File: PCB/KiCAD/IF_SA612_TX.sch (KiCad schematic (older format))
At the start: 19 parts, among them J3 MIC, Q10 MMBT4401LT1G, U8 LM78L06, U9 SA612

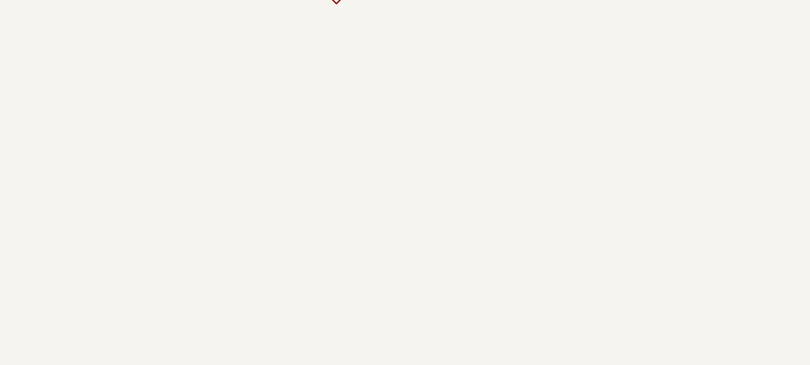
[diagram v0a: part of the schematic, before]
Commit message: diode mixer on discrete components, begin move to DragonFly libs
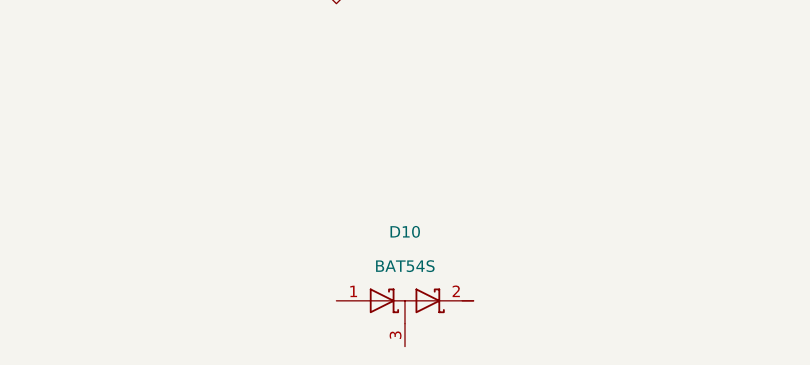
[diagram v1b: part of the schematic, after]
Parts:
- added D10: BAT54S, TO_SOT_Packages_SMD:SOT-23, symbol D_Schottky_x2_Serial_AKC
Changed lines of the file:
@@
 EESchema Schematic File Version 2
 LIBS:DragonFly-rescue
-LIBS:bee-rescue
 LIBS:power
 LIBS:device
@@
 $EndDescr
 $Comp
-L GND #PWR72
+L GND #PWR078
 U 1 1 58E1AB18
 P 1750 2050
-F 0 "#PWR72" H 1750 1800 50  0001 C CNN
+F 0 "#PWR078" H 1750 1800 50  0001 C CNN
 F 1 "GND" H 1750 1900 50  0001 C CNN
 F 2 "" H 1750 2050 50  0000 C CNN
@@
 $EndComp
 $Comp
-L GND #PWR74
+L GND #PWR079
 U 1 1 58E1AB3A
 P 2950 4000
-F 0 "#PWR74" H 2950 3750 50  0001 C CNN
+F 0 "#PWR079" H 2950 3750 50  0001 C CNN
 F 1 "GND" H 2950 3850 50  0001 C CNN
 F 2 "" H 2950 4000 50  0000 C CNN
@@
 $EndComp
 $Comp
-L GND #PWR73
+L GND #PWR080
 U 1 1 58E1AB40
 P 2200 4000
-F 0 "#PWR73" H 2200 3750 50  0001 C CNN
+F 0 "#PWR080" H 2200 3750 50  0001 C CNN
 F 1 "GND" H 2200 3850 50  0001 C CNN
 F 2 "" H 2200 4000 50  0000 C CNN
@@
 $EndComp
 $Comp
-L GND #PWR76
+L GND #PWR081
 U 1 1 58E1AB6A
 P 3250 1450
-F 0 "#PWR76" H 3250 1200 50  0001 C CNN
+F 0 "#PWR081" H 3250 1200 50  0001 C CNN
 F 1 "GND" H 3250 1300 50  0001 C CNN
 F 2 "" H 3250 1450 50  0000 C CNN
@@
 $EndComp
 $Comp
-L GND #PWR80
+L GND #PWR082
 U 1 1 58E1AB77
 P 5100 2050
-F 0 "#PWR80" H 5100 1800 50  0001 C CNN
+F 0 "#PWR082" H 5100 1800 50  0001 C CNN
 F 1 "GND" H 5100 1900 50  0001 C CNN
 F 2 "" H 5100 2050 50  0000 C CNN
@@
 $EndComp
 $Comp
-L GND #PWR79
+L GND #PWR083
 U 1 1 58E1AB7D
 P 4950 2850
-F 0 "#PWR79" H 4950 2600 50  0001 C CNN
+F 0 "#PWR083" H 4950 2600 50  0001 C CNN
 F 1 "GND" H 4950 2700 50  0001 C CNN
 F 2 "" H 4950 2850 50  0000 C CNN
@@
 $EndComp
 $Comp
-L GND #PWR78
+L GND #PWR084
 U 1 1 58E1ABAE
 P 4800 1500
-F 0 "#PWR78" H 4800 1250 50  0001 C CNN
+F 0 "#PWR084" H 4800 1250 50  0001 C CNN
 F 1 "GND" H 4800 1350 50  0001 C CNN
 F 2 "" H 4800 1500 50  0000 C CNN
@@
 $EndComp
 $Comp
-L GND #PWR81
+L GND #PWR085
 U 1 1 58E1ABB4
 P 5300 1500
-F 0 "#PWR81" H 5300 1250 50  0001 C CNN
+F 0 "#PWR085" H 5300 1250 50  0001 C CNN
 F 1 "GND" H 5300 1350 50  0001 C CNN
 F 2 "" H 5300 1500 50  0000 C CNN
@@
 Connection ~ 5950 2250
 $Comp
-L GND #PWR82
+L GND #PWR086
 U 1 1 58E1ABEC
 P 5850 2400
-F 0 "#PWR82" H 5850 2150 50  0001 C CNN
+F 0 "#PWR086" H 5850 2150 50  0001 C CNN
 F 1 "GND" H 5850 2250 50  0001 C CNN
 F 2 "" H 5850 2400 50  0000 C CNN
@@
 	5850 2350 6050 2350
 $Comp
-L GND #PWR83
+L GND #PWR087
 U 1 1 58E1ABF4
 P 5850 2950
-F 0 "#PWR83" H 5850 2700 50  0001 C CNN
+F 0 "#PWR087" H 5850 2700 50  0001 C CNN
 F 1 "GND" H 5850 2800 50  0001 C CNN
 F 2 "" H 5850 2950 50  0000 C CNN
@@
 	2950 3800 2950 4000
 $Comp
-L GND #PWR77
+L GND #PWR088
 U 1 1 60FE7FDF
 P 3500 4250
-F 0 "#PWR77" H 3500 4000 50  0001 C CNN
+F 0 "#PWR088" H 3500 4000 50  0001 C CNN
 F 1 "GND" H 3500 4100 50  0001 C CNN
 F 2 "" H 3500 4250 50  0000 C CNN
@@
 $EndComp
 $Comp
-L GND #PWR75
+L GND #PWR089
 U 1 1 60FE877B
 P 3100 2600
-F 0 "#PWR75" H 3100 2350 50  0001 C CNN
+F 0 "#PWR089" H 3100 2350 50  0001 C CNN
 F 1 "GND" H 3100 2450 50  0001 C CNN
 F 2 "" H 3100 2600 50  0000 C CNN
@@
 Wire Wire Line
 	3500 2700 3500 3050
+$Comp
+L D_Schottky_x2_Serial_AKC D10
+U 1 1 612298E2
+P 3800 5650
+F 0 "D10" H 3800 5950 50  0000 C CNN
+F 1 "BAT54S" H 3800 5800 50  0000 C CNN
+F 2 "TO_SOT_Packages_SMD:SOT-23" H 3800 5650 50  0001 C CNN
+F 3 "" H 3800 5650 50  0000 C CNN
+	1    3800 5650
+	1    0    0    -1
+$EndComp
 $EndSCHEMATC

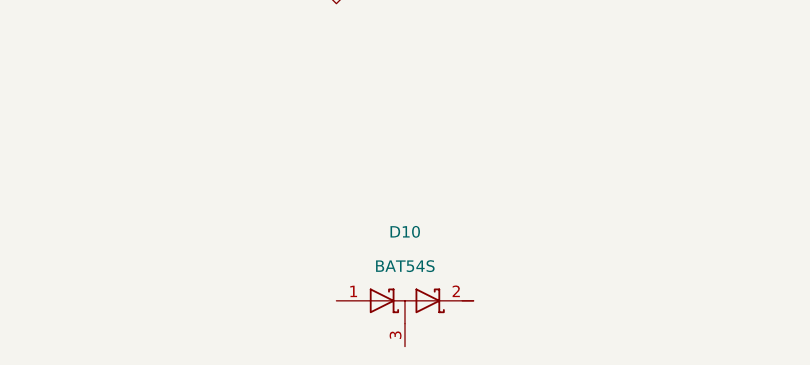
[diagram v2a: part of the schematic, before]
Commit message: PCB read works, layout BPF
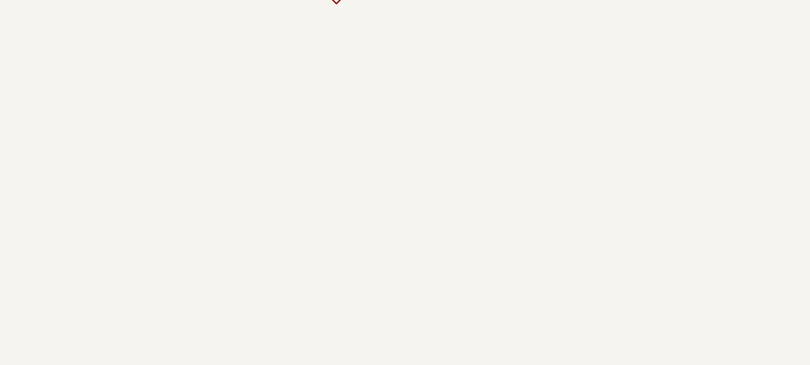
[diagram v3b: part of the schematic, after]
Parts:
- removed D10: BAT54S, TO_SOT_Packages_SMD:SOT-23, symbol D_Schottky_x2_Serial_AKC
- C32, C33, C35, C36, C38, C42: footprint Capacitors_SMD:C_0603_HandSoldering -> DragonFly:C_0603_HandSoldering
- C40: footprint Capacitors_THT:CP_Radial_D6.3mm_P2.50mm -> DragonFly:CP_Radial_D6.3mm_P2.50mm
- D5, Q10: footprint TO_SOT_Packages_SMD:SOT-23 -> DragonFly:SOT-23
- U8: footprint TO_SOT_Packages_THT:TO-92_Molded_Wide_Oval -> DragonFly:TO-92_Molded_Wide_Oval
- U9: footprint Housings_SOIC:SOIC-8_3.9x4.9mm_Pitch1.27mm -> DragonFly:SOIC-8_3.9x4.9mm_Pitch1.27mm
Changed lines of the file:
@@
 $EndDescr
 $Comp
-L GND #PWR78
+L GND #PWR078
 U 1 1 58E1AB18
 P 1750 2050
-F 0 "#PWR78" H 1750 1800 50  0001 C CNN
+F 0 "#PWR078" H 1750 1800 50  0001 C CNN
 F 1 "GND" H 1750 1900 50  0001 C CNN
 F 2 "" H 1750 2050 50  0000 C CNN
@@
 F 0 "C33" H 2300 3850 50  0000 L CNN
 F 1 "100nF" H 2300 3950 50  0000 L CNN
-F 2 "Capacitors_SMD:C_0603_HandSoldering" H 2200 3900 50  0001 C CNN
+F 2 "DragonFly:C_0603_HandSoldering" H 2200 3900 50  0001 C CNN
 F 3 "" H 2200 3900 50  0000 C CNN
 	1    2200 3900
@@
 $EndComp
 $Comp
-L GND #PWR80
+L GND #PWR079
 U 1 1 58E1AB3A
 P 2950 4000
-F 0 "#PWR80" H 2950 3750 50  0001 C CNN
+F 0 "#PWR079" H 2950 3750 50  0001 C CNN
 F 1 "GND" H 2950 3850 50  0001 C CNN
 F 2 "" H 2950 4000 50  0000 C CNN
@@
 $EndComp
 $Comp
-L GND #PWR79
+L GND #PWR080
 U 1 1 58E1AB40
 P 2200 4000
-F 0 "#PWR79" H 2200 3750 50  0001 C CNN
+F 0 "#PWR080" H 2200 3750 50  0001 C CNN
 F 1 "GND" H 2200 3850 50  0001 C CNN
 F 2 "" H 2200 4000 50  0000 C CNN
@@
 F 0 "U9" H 4350 3250 50  0000 C CNN
 F 1 "SA612" H 4350 2650 50  0000 C CNN
-F 2 "Housings_SOIC:SOIC-8_3.9x4.9mm_Pitch1.27mm" H 4350 2800 60  0001 C CNN
+F 2 "DragonFly:SOIC-8_3.9x4.9mm_Pitch1.27mm" H 4350 2800 60  0001 C CNN
 F 3 "" H 4350 2800 60  0000 C CNN
 	1    4350 2800
@@
 F 0 "Q10" H 2950 2900 50  0000 L CNN
 F 1 "MMBT4401LT1G" H 2950 2800 50  0000 L CNN
-F 2 "TO_SOT_Packages_SMD:SOT-23" H 2950 2725 50  0001 L CIN
+F 2 "DragonFly:SOT-23" H 2950 2725 50  0001 L CIN
 F 3 "" H 2750 2800 50  0000 L CNN
 	1    2750 2800
@@
 F 0 "D5" H 2200 1850 50  0000 C CNN
 F 1 "BAT54S" H 2200 1700 50  0000 C CNN
-F 2 "TO_SOT_Packages_SMD:SOT-23" H 2200 1550 50  0001 C CNN
+F 2 "DragonFly:SOT-23" H 2200 1550 50  0001 C CNN
 F 3 "" H 2200 1550 50  0000 C CNN
 	1    2200 1550
@@
 F 0 "U8" H 3250 1500 50  0000 C CNN
 F 1 "LM78L06" H 3250 1400 50  0000 C CNN
-F 2 "TO_SOT_Packages_THT:TO-92_Molded_Wide_Oval" H 3250 1200 50  0001 C CNN
+F 2 "DragonFly:TO-92_Molded_Wide_Oval" H 3250 1200 50  0001 C CNN
 F 3 "" H 3250 1200 50  0000 C CNN
 	1    3250 1200
@@
 $EndComp
 $Comp
-L GND #PWR82
+L GND #PWR081
 U 1 1 58E1AB6A
 P 3250 1450
-F 0 "#PWR82" H 3250 1200 50  0001 C CNN
+F 0 "#PWR081" H 3250 1200 50  0001 C CNN
 F 1 "GND" H 3250 1300 50  0001 C CNN
 F 2 "" H 3250 1450 50  0000 C CNN
@@
 $EndComp
 $Comp
-L GND #PWR86
+L GND #PWR082
 U 1 1 58E1AB77
 P 5100 2050
-F 0 "#PWR86" H 5100 1800 50  0001 C CNN
+F 0 "#PWR082" H 5100 1800 50  0001 C CNN
 F 1 "GND" H 5100 1900 50  0001 C CNN
 F 2 "" H 5100 2050 50  0000 C CNN
@@
 $EndComp
 $Comp
-L GND #PWR85
+L GND #PWR083
 U 1 1 58E1AB7D
 P 4950 2850
-F 0 "#PWR85" H 4950 2600 50  0001 C CNN
+F 0 "#PWR083" H 4950 2600 50  0001 C CNN
 F 1 "GND" H 4950 2700 50  0001 C CNN
 F 2 "" H 4950 2850 50  0000 C CNN
@@
 F 0 "C38" H 4550 1400 50  0000 L CNN
 F 1 "100nF" H 4550 1500 50  0000 L CNN
-F 2 "Capacitors_SMD:C_0603_HandSoldering" H 4800 1400 50  0001 C CNN
+F 2 "DragonFly:C_0603_HandSoldering" H 4800 1400 50  0001 C CNN
 F 3 "" H 4800 1400 50  0000 C CNN
 	1    4800 1400
@@
 $EndComp
 $Comp
-L GND #PWR84
+L GND #PWR084
 U 1 1 58E1ABAE
 P 4800 1500
-F 0 "#PWR84" H 4800 1250 50  0001 C CNN
+F 0 "#PWR084" H 4800 1250 50  0001 C CNN
 F 1 "GND" H 4800 1350 50  0001 C CNN
 F 2 "" H 4800 1500 50  0000 C CNN
@@
 $EndComp
 $Comp
-L GND #PWR87
+L GND #PWR085
 U 1 1 58E1ABB4
 P 5300 1500
-F 0 "#PWR87" H 5300 1250 50  0001 C CNN
+F 0 "#PWR085" H 5300 1250 50  0001 C CNN
 F 1 "GND" H 5300 1350 50  0001 C CNN
 F 2 "" H 5300 1500 50  0000 C CNN
@@
 F 0 "C32" H 1850 1950 50  0000 L CNN
 F 1 "100nF" H 1800 2050 50  0000 L CNN
-F 2 "Capacitors_SMD:C_0603_HandSoldering" H 1750 1950 50  0001 C CNN
+F 2 "DragonFly:C_0603_HandSoldering" H 1750 1950 50  0001 C CNN
 F 3 "" H 1750 1950 50  0000 C CNN
 	1    1750 1950
@@
 F 0 "C40" H 5400 1400 50  0000 L CNN
 F 1 "100µF" H 5400 1300 50  0000 L CNN
-F 2 "Capacitors_THT:CP_Radial_D6.3mm_P2.50mm" H 5300 1400 50  0001 C CNN
+F 2 "DragonFly:CP_Radial_D6.3mm_P2.50mm" H 5300 1400 50  0001 C CNN
 F 3 "" H 5300 1400 50  0000 C CNN
 	1    5300 1400
@@
 F 0 "C42" H 5600 2800 50  0000 L CNN
 F 1 "10nF" H 5550 2900 50  0000 L CNN
-F 2 "Capacitors_SMD:C_0603_HandSoldering" H 5850 2850 50  0001 C CNN
+F 2 "DragonFly:C_0603_HandSoldering" H 5850 2850 50  0001 C CNN
 F 3 "" H 5850 2850 50  0000 C CNN
 	1    5850 2850
@@
 Connection ~ 5950 2250
 $Comp
-L GND #PWR88
+L GND #PWR086
 U 1 1 58E1ABEC
 P 5850 2400
-F 0 "#PWR88" H 5850 2150 50  0001 C CNN
+F 0 "#PWR086" H 5850 2150 50  0001 C CNN
 F 1 "GND" H 5850 2250 50  0001 C CNN
 F 2 "" H 5850 2400 50  0000 C CNN
@@
 	5850 2350 6050 2350
 $Comp
-L GND #PWR89
+L GND #PWR087
 U 1 1 58E1ABF4
 P 5850 2950
-F 0 "#PWR89" H 5850 2700 50  0001 C CNN
+F 0 "#PWR087" H 5850 2700 50  0001 C CNN
 F 1 "GND" H 5850 2800 50  0001 C CNN
 F 2 "" H 5850 2950 50  0000 C CNN
@@
 	2950 3800 2950 4000
 $Comp
-L GND #PWR83
+L GND #PWR088
 U 1 1 60FE7FDF
 P 3500 4250
-F 0 "#PWR83" H 3500 4000 50  0001 C CNN
+F 0 "#PWR088" H 3500 4000 50  0001 C CNN
 F 1 "GND" H 3500 4100 50  0001 C CNN
 F 2 "" H 3500 4250 50  0000 C CNN
@@
 F 0 "C36" H 3200 3100 50  0000 L CNN
 F 1 "10nF" H 3150 3200 50  0000 L CNN
-F 2 "Capacitors_SMD:C_0603_HandSoldering" H 3500 3150 50  0001 C CNN
+F 2 "DragonFly:C_0603_HandSoldering" H 3500 3150 50  0001 C CNN
 F 3 "" H 3500 3150 50  0000 C CNN
 	1    3500 3150
@@
 F 0 "C35" V 3000 2550 50  0000 L CNN
 F 1 "100nF" V 3150 2550 50  0000 L CNN
-F 2 "Capacitors_SMD:C_0603_HandSoldering" H 3300 2600 50  0001 C CNN
+F 2 "DragonFly:C_0603_HandSoldering" H 3300 2600 50  0001 C CNN
 F 3 "" H 3300 2600 50  0000 C CNN
 	1    3300 2600
@@
 $EndComp
 $Comp
-L GND #PWR81
+L GND #PWR089
 U 1 1 60FE877B
 P 3100 2600
-F 0 "#PWR81" H 3100 2350 50  0001 C CNN
+F 0 "#PWR089" H 3100 2350 50  0001 C CNN
 F 1 "GND" H 3100 2450 50  0001 C CNN
 F 2 "" H 3100 2600 50  0000 C CNN
@@
 Wire Wire Line
 	3500 2700 3500 3050
-$Comp
-L D_Schottky_x2_Serial_AKC D10
-U 1 1 612298E2
-P 3800 5650
-F 0 "D10" H 3800 5950 50  0000 C CNN
-F 1 "BAT54S" H 3800 5800 50  0000 C CNN
-F 2 "TO_SOT_Packages_SMD:SOT-23" H 3800 5650 50  0001 C CNN
-F 3 "" H 3800 5650 50  0000 C CNN
-	1    3800 5650
-	1    0    0    -1
-$EndComp
 $EndSCHEMATC
